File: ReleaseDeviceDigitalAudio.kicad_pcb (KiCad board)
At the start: 2 copper layers, 132 x 68.5 mm, 183 parts, among them J1 AudioJack3, J10 UIBoardCON2, J2 AudioJack3, J3 AudioJack3, J4 AudioJack3, J5 AudioJack3, J6 ATMEGA_PROG, J7 SignalStrength, J8 UIBoardCON1, J9 Conn_01x03, Q1 BSS314PEH6327XTSA1, Q3 SQ2362ES-T1_GE3, Q4 SQD50P06-15L_GE3, SW1 KeySwitch, U1 ATmega4809-A, U10 ULN2003F12FN-7, U11 ULN2003F12FN-7, U12 ULN2003F12FN-7, U13 ULN2003F12FN-7, U14 MAX98089ETN+, U15 SN74LV1T126, U16 SN74LV1T126, U17 BM83SM1-00TA, U18 PCF85063A, U2 VOMA617A, U3 VOMA617A, U4 LM53635LQRNL*Q1, U5 TLVH431AQDBVRQ1, U6 LM74610-Q1, U7 Compute_Module_4_Connectors, U8 CD4514BM, U9 CD4511BPWR, Y1 9HT12

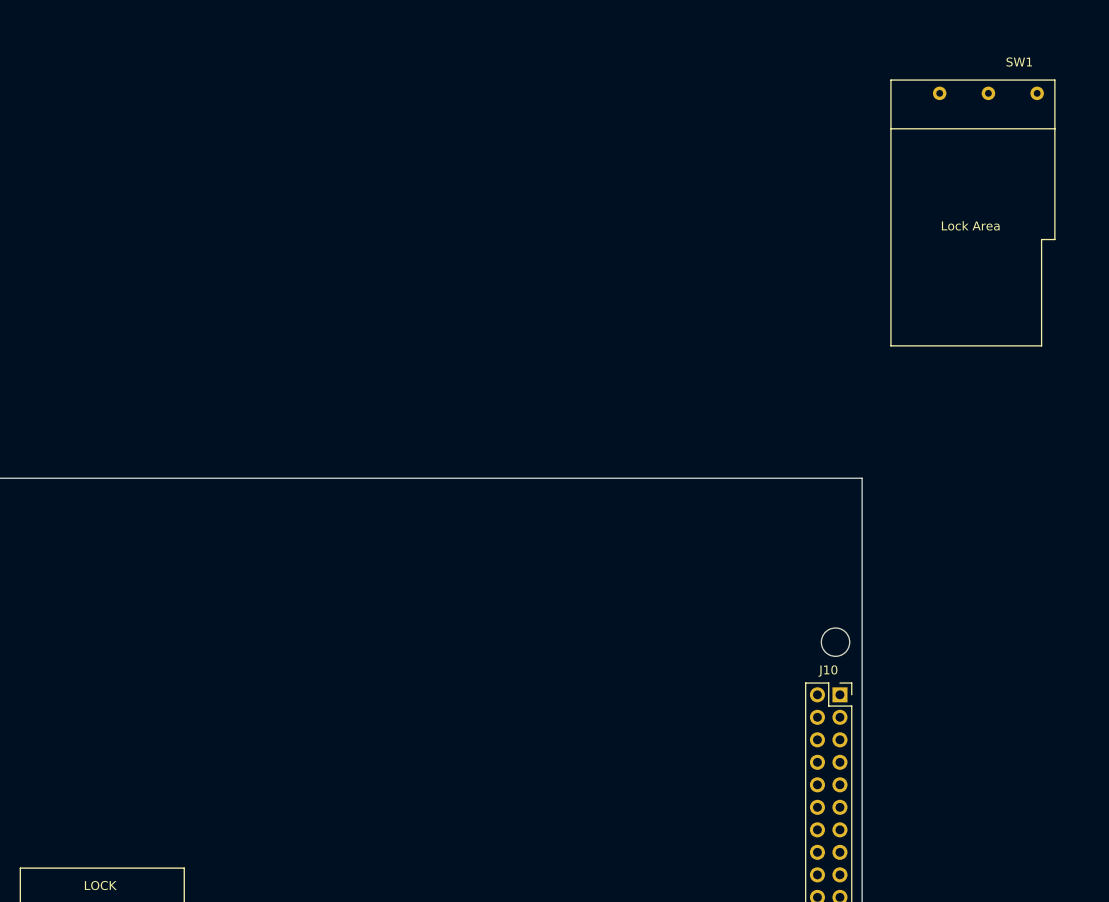
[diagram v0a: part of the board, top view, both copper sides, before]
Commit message: - SW1 entfernt
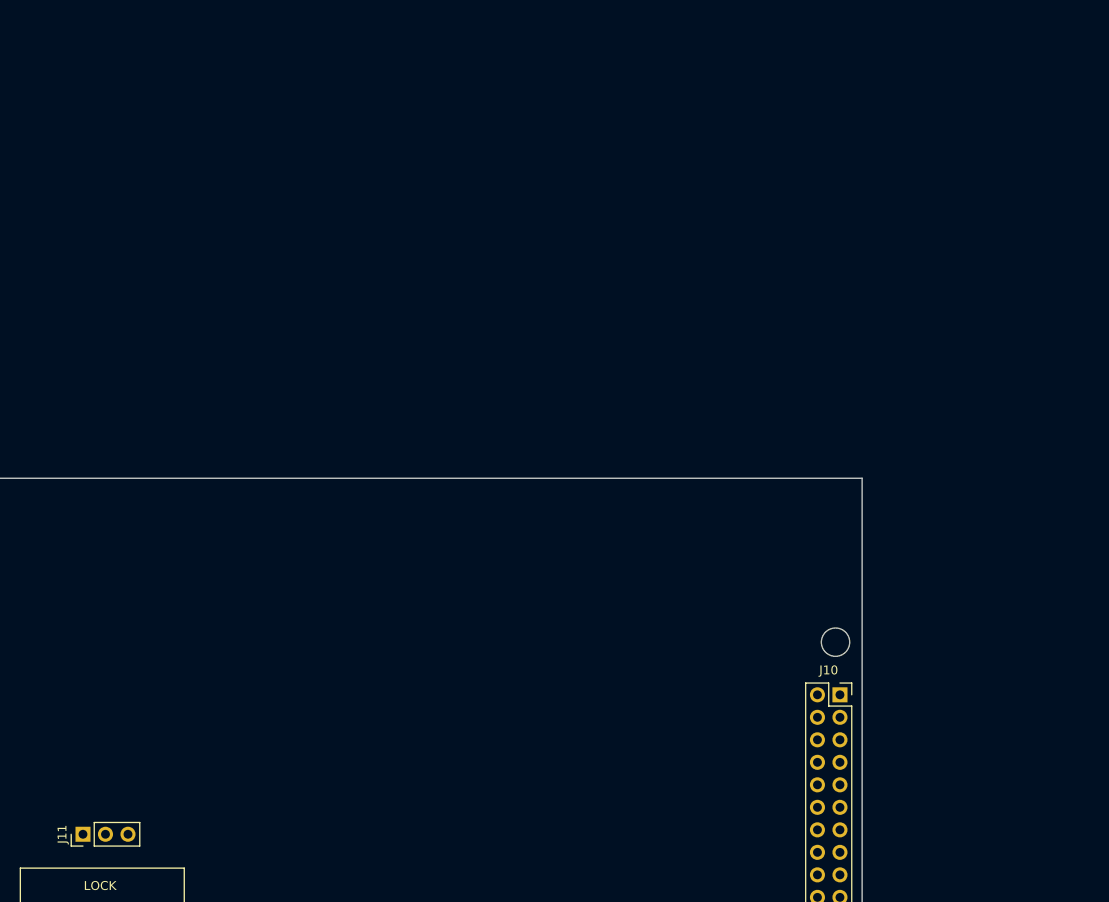
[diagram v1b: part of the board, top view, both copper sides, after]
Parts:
- removed SW1: KeySwitch, TeKaDe:KeySwitch
- added J11: KeySwitch, Connector_PinHeader_2.54mm:PinHeader_1x03_P2.54mm_Vertical, F.Cu at (128.1, 101.2)
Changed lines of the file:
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@@
     (add_net VPP)
+  )
+  (module Connector_PinHeader_2.54mm:PinHeader_1x03_P2.54mm_Vertical (layer F.Cu)
+    (at 128.069 101.179 90)
+    (descr "Through hole straight pin header, 1x03, 2.54mm pitch, single row")
+    (tags "Through hole pin header THT 1x03 2.54mm single row")
+    (fp_text reference J11 (at 0 -2.33 90) (layer F.SilkS)
+      (effects (font (size 1 1) (thickness 0.15)))
+    )
+    (fp_text value KeySwitch (at 0 7.41 90) (layer F.Fab)
+      (effects (font (size 1 1) (thickness 0.15)))
+    )
+    (fp_text user %R (at 0 2.54) (layer F.Fab)
+      (effects (font (size 1 1) (thickness 0.15)))
+    )
+    (fp_line (start 1.8 -1.8) (end -1.8 -1.8) (layer F.CrtYd) (width 0.05))
+    (fp_line (start 1.8 6.85) (end 1.8 -1.8) (layer F.CrtYd) (width 0.05))
+    (fp_line (start -1.8 6.85) (end 1.8 6.85) (layer F.CrtYd) (width 0.05))
+    (fp_line (start -1.8 -1.8) (end -1.8 6.85) (layer F.CrtYd) (width 0.05))
+    (fp_line (start -1.33 -1.33) (end 0 -1.33) (layer F.SilkS) (width 0.12))
+    (fp_line (start -1.33 0) (end -1.33 -1.33) (layer F.SilkS) (width 0.12))
+    (fp_line (start -1.33 1.27) (end 1.33 1.27) (layer F.SilkS) (width 0.12))
+    (fp_line (start 1.33 1.27) (end 1.33 6.41) (layer F.SilkS) (width 0.12))
+    (fp_line (start -1.33 1.27) (end -1.33 6.41) (layer F.SilkS) (width 0.12))
+    (fp_line (start -1.33 6.41) (end 1.33 6.41) (layer F.SilkS) (width 0.12))
+    (fp_line (start -1.27 -0.635) (end -0.635 -1.27) (layer F.Fab) (width 0.1))
+    (fp_line (start -1.27 6.35) (end -1.27 -0.635) (layer F.Fab) (width 0.1))
+    (fp_line (start 1.27 6.35) (end -1.27 6.35) (layer F.Fab) (width 0.1))
+    (fp_line (start 1.27 -1.27) (end 1.27 6.35) (layer F.Fab) (width 0.1))
+    (fp_line (start -0.635 -1.27) (end 1.27 -1.27) (layer F.Fab) (width 0.1))
+    (pad 3 thru_hole oval (at 0 5.08 90) (size 1.7 1.7) (drill 1) (layers *.Cu *.Mask)
+      (net 2 GND))
+    (pad 2 thru_hole oval (at 0 2.54 90) (size 1.7 1.7) (drill 1) (layers *.Cu *.Mask)
+      (net 82 /ControllerUIBoard/KeySwitchB))
+    (pad 1 thru_hole rect (at 0 0 90) (size 1.7 1.7) (drill 1) (layers *.Cu *.Mask)
+      (net 83 /ControllerUIBoard/KeySwitchA))
+    (model ${KISYS3DMOD}/Connector_PinHeader_2.54mm.3dshapes/PinHeader_1x03_P2.54mm_Vertical.wrl
+      (at (xyz 0 0 0))
+      (scale (xyz 1 1 1))
+      (rotate (xyz 0 0 0))
+    )
   )
   (module Package_SO:TSSOP-16_4.4x5mm_P0.65mm (layer F.Cu)
@@
     )
   )
-  (module TeKaDe:KeySwitch (layer F.Cu)
-    (at 219.255 46.061)
-    (fp_text reference SW1 (at 14.5 -32) (layer F.SilkS)
-      (effects (font (size 1 1) (thickness 0.15)))
-    )
-    (fp_text value KeySwitch (at 6.5 -32) (layer F.Fab)
-      (effects (font (size 1 1) (thickness 0.15)))
-    )
-    (fp_line (start 18.5 -24.5) (end 0 -24.5) (layer F.SilkS) (width 0.12))
-    (fp_line (start 0 -30) (end 0 0) (layer F.SilkS) (width 0.12))
-    (fp_line (start 18.5 -30) (end 0 -30) (layer F.SilkS) (width 0.12))
-    (fp_line (start 18.5 -24.5) (end 18.5 -30) (layer F.SilkS) (width 0.12))
-    (fp_line (start 18.5 -12) (end 18.5 -24.5) (layer F.SilkS) (width 0.12))
-    (fp_line (start 17 -12) (end 18.5 -12) (layer F.SilkS) (width 0.12))
-    (fp_line (start 17 0) (end 17 -12) (layer F.SilkS) (width 0.12))
-    (fp_line (start 0 0) (end 17 0) (layer F.SilkS) (width 0.12))
-    (fp_text user "Lock Area" (at 9 -13.5) (layer F.SilkS)
-      (effects (font (size 1 1) (thickness 0.15)))
-    )
-    (pad 3 thru_hole circle (at 16.5 -28.5) (size 1.524 1.524) (drill 0.762) (layers *.Cu *.Mask)
-      (net 2 GND))
-    (pad 2 thru_hole circle (at 11 -28.5) (size 1.524 1.524) (drill 0.762) (layers *.Cu *.Mask)
-      (net 82 /ControllerUIBoard/KeySwitchB))
-    (pad 1 thru_hole circle (at 5.5 -28.5) (size 1.524 1.524) (drill 0.762) (layers *.Cu *.Mask)
-      (net 83 /ControllerUIBoard/KeySwitchA))
-  )
   (module MountingHole:MountingHole_2.5mm locked (layer F.Cu)

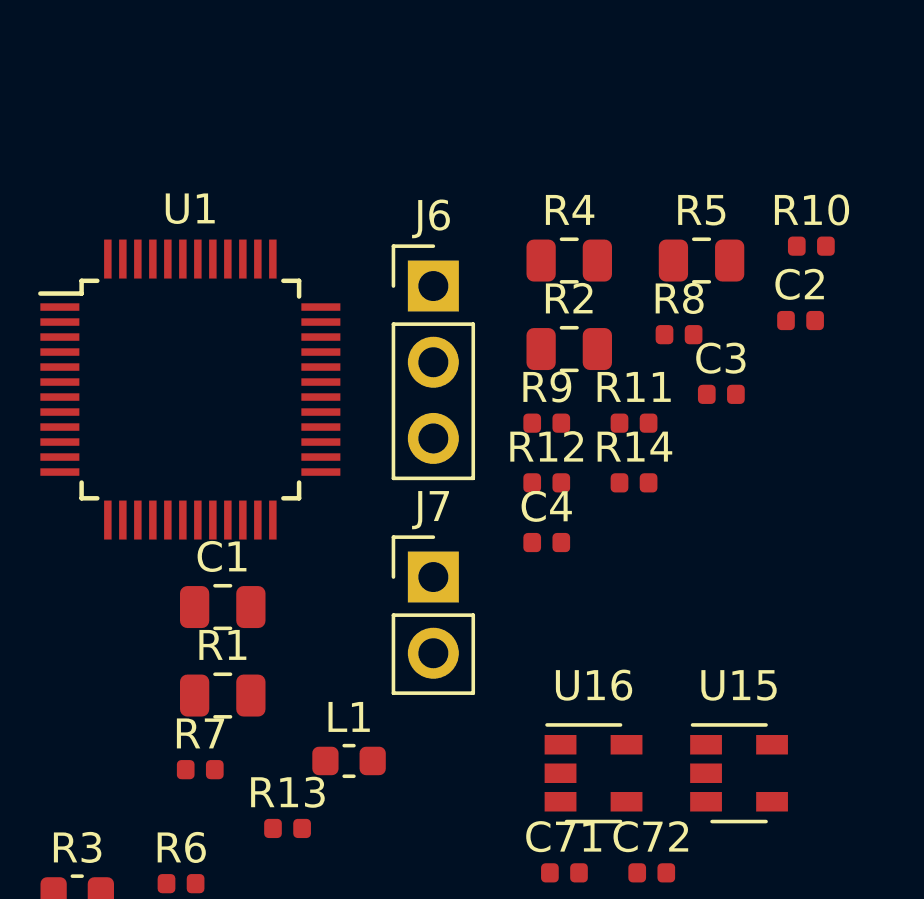
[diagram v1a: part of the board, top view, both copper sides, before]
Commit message: - Wert und Footprint der LED Vorwiderstaende angepasst
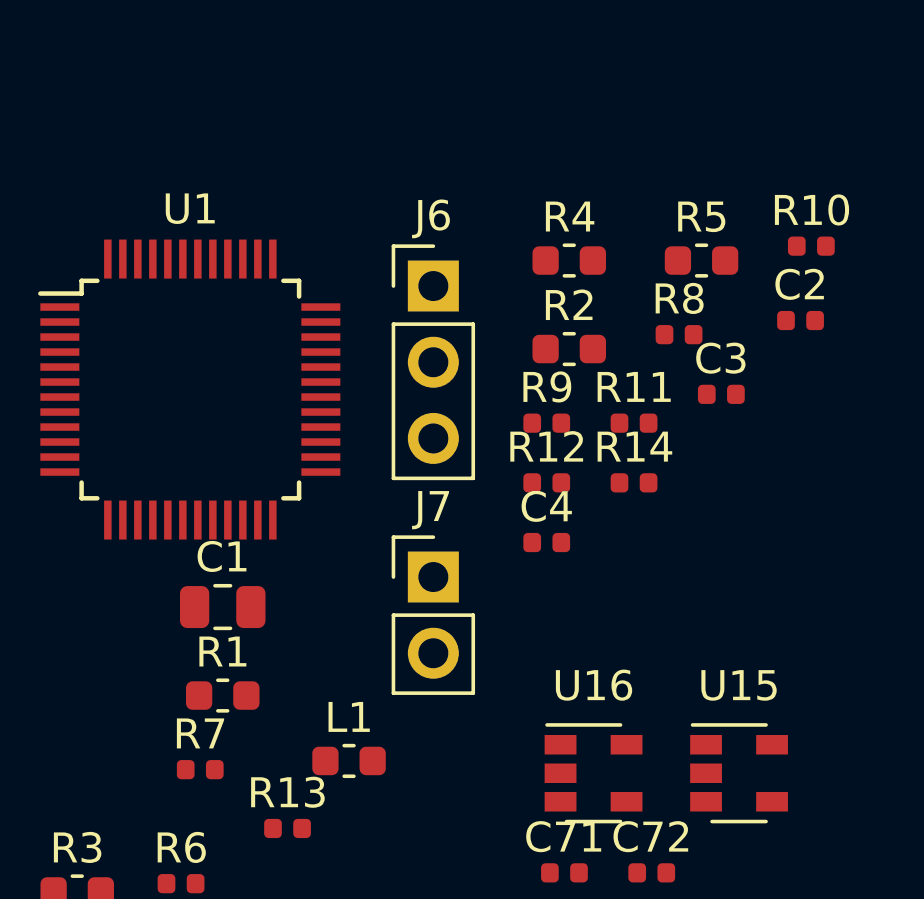
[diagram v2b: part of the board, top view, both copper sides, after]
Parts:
- R1, R2, R4, R5: value 392R/1% -> 150R/1%; footprint Resistor_SMD:R_0805_2012Metric -> Resistor_SMD:R_0603_1608Metric

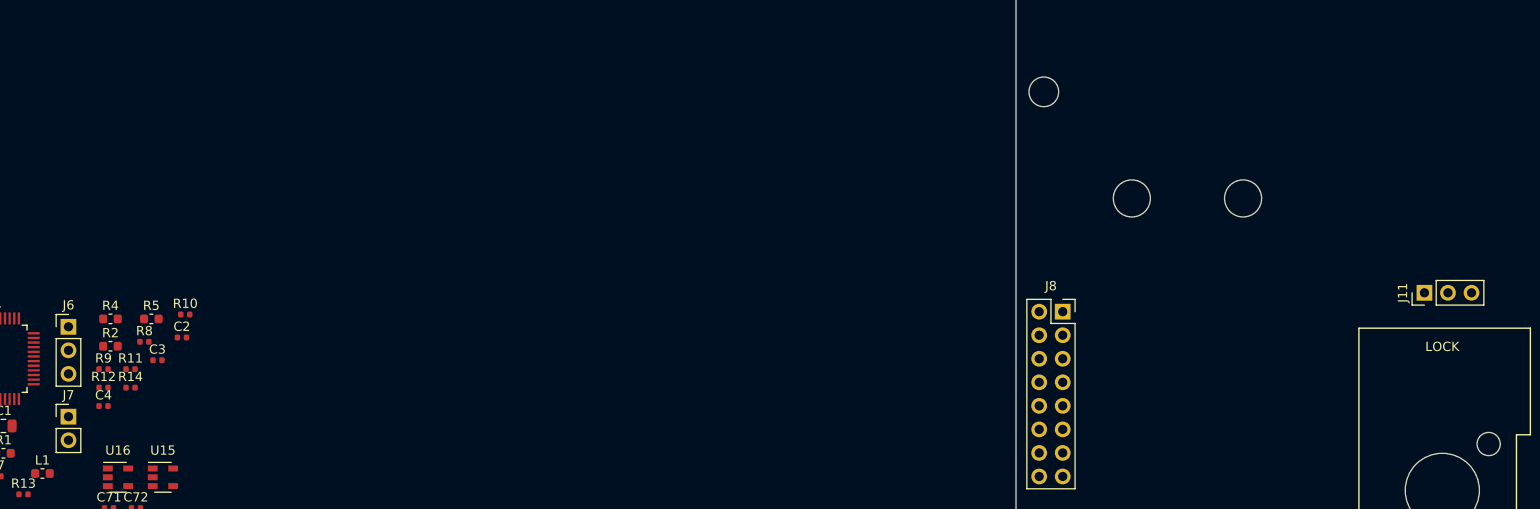
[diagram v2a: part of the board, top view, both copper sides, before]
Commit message: - Steckverbinder Signal und Lock aktualisiert
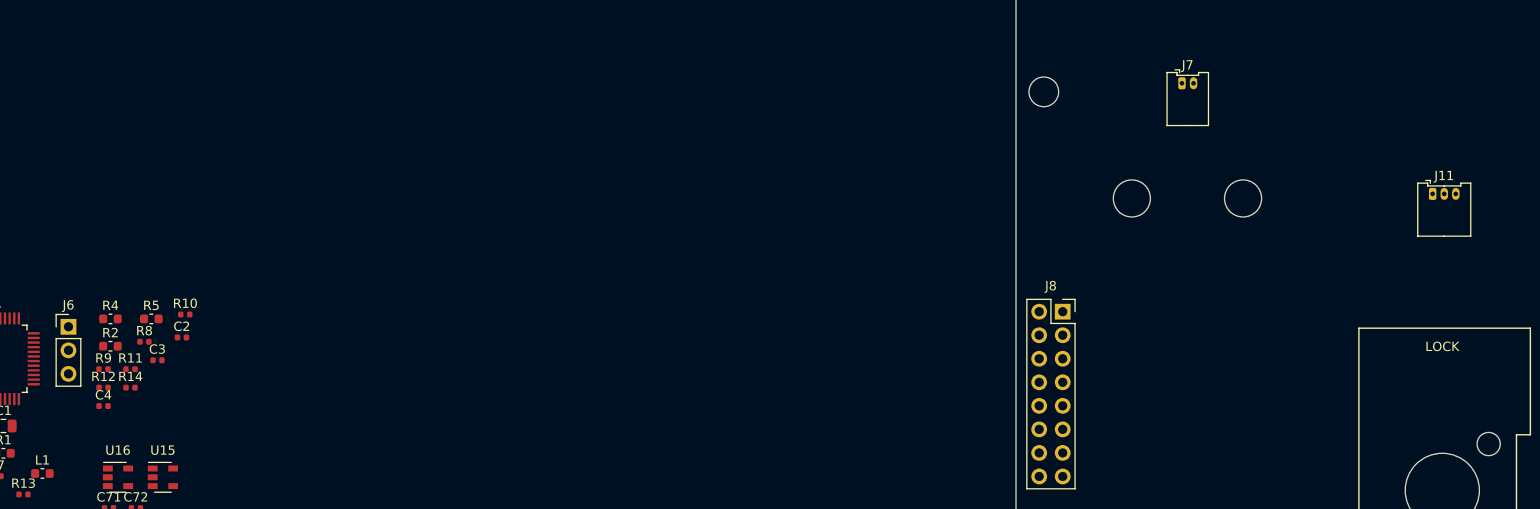
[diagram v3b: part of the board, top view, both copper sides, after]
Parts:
- J11: footprint Connector_PinHeader_2.54mm:PinHeader_1x03_P2.54mm_Vertical -> Connector_Molex:Molex_PicoBlade_53048-0310_1x03_P1.25mm_Horizontal
- J7: footprint Connector_PinHeader_2.54mm:PinHeader_1x02_P2.54mm_Vertical -> Connector_Molex:Molex_PicoBlade_53048-0210_1x02_P1.25mm_Horizontal
- moved J7 125.4 mm to (101.9, 78.6)
- moved J11 10.7 mm to (129.0, 90.5), turned to 0 degrees

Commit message: - vorlaeufige Bauteil Positionierung
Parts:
- J6: footprint Connector_PinHeader_2.54mm:PinHeader_1x03_P2.54mm_Vertical -> Connector_PinHeader_2.54mm:PinHeader_1x03_P2.54mm_Horizontal
- J7, J9: moved to B.Cu
- moved D1 239.8 mm to (120.0, 27.0), turned to 180 degrees
- moved J9 236.4 mm to (119.0, 35.9), turned to 180 degrees
- moved U6 227.1 mm to (111.8, 27.5), turned to 180 degrees
- moved C30 215.9 mm to (105.0, 28.5), turned to 180 degrees
- moved C11 211.6 mm to (99.4, 26.3), turned to 180 degrees
- moved R27 208.1 mm to (100.2, 29.4), turned to 180 degrees
- moved C6 204.8 mm to (94.4, 26.4), turned to 180 degrees
- moved C26 200.4 mm to (95.2, 30.0), turned to 180 degrees
- moved Q4 199.4 mm to (96.4, 36.3), turned to 180 degrees
- moved C22 199.4 mm to (90.0, 26.4), turned to 180 degrees
- moved L2 198.3 mm to (105.6, 47.1), turned to 180 degrees
- moved R32 196.6 mm to (147.0, 110.5), turned to 180 degrees
- moved R29 194.9 mm to (85.8, 26.1), turned to 180 degrees
- moved C13 193.3 mm to (89.6, 30.0), turned to 180 degrees
- moved C37 193.3 mm to (150.0, 121.8)
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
